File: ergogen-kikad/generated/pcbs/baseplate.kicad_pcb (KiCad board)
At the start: 2 copper layers, 111.1 x 55 mm, 22 parts, among them J1 Header clearance

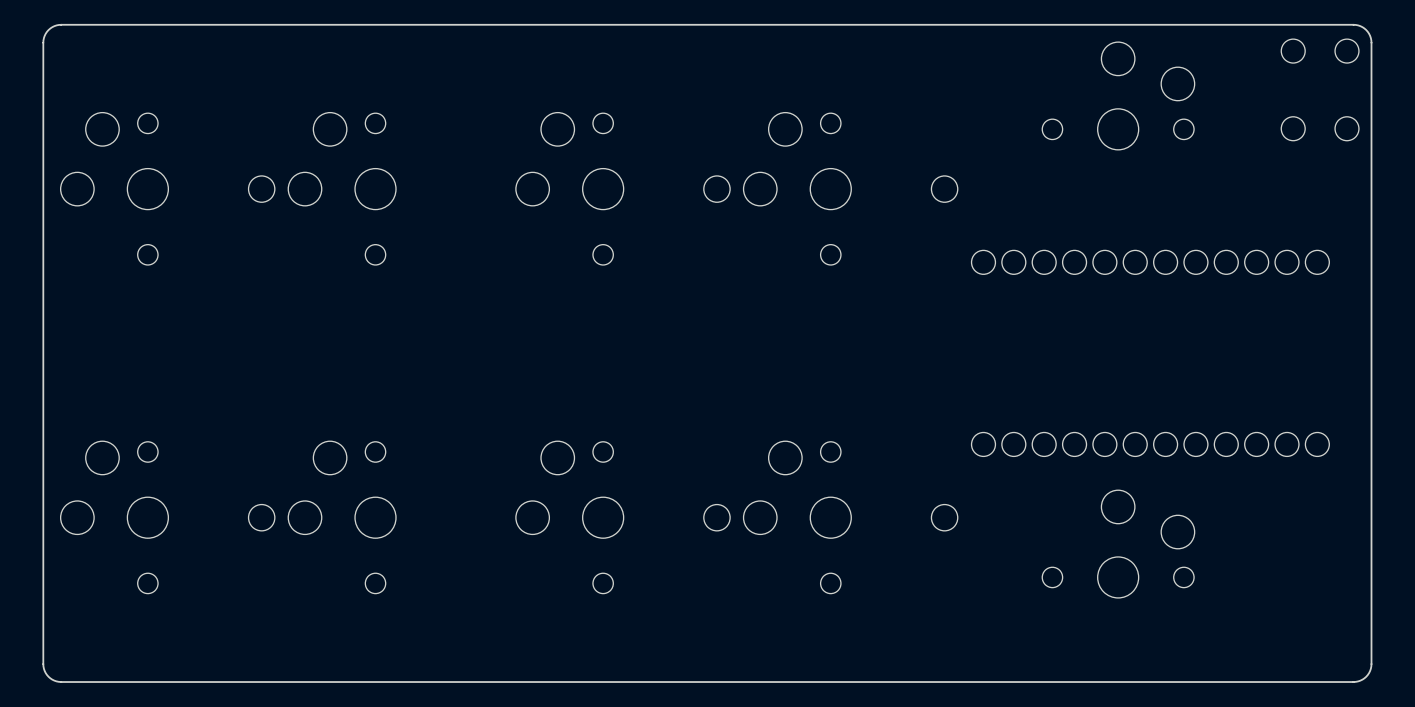
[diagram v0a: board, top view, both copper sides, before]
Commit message: Socket nice!view directly and lower reset button
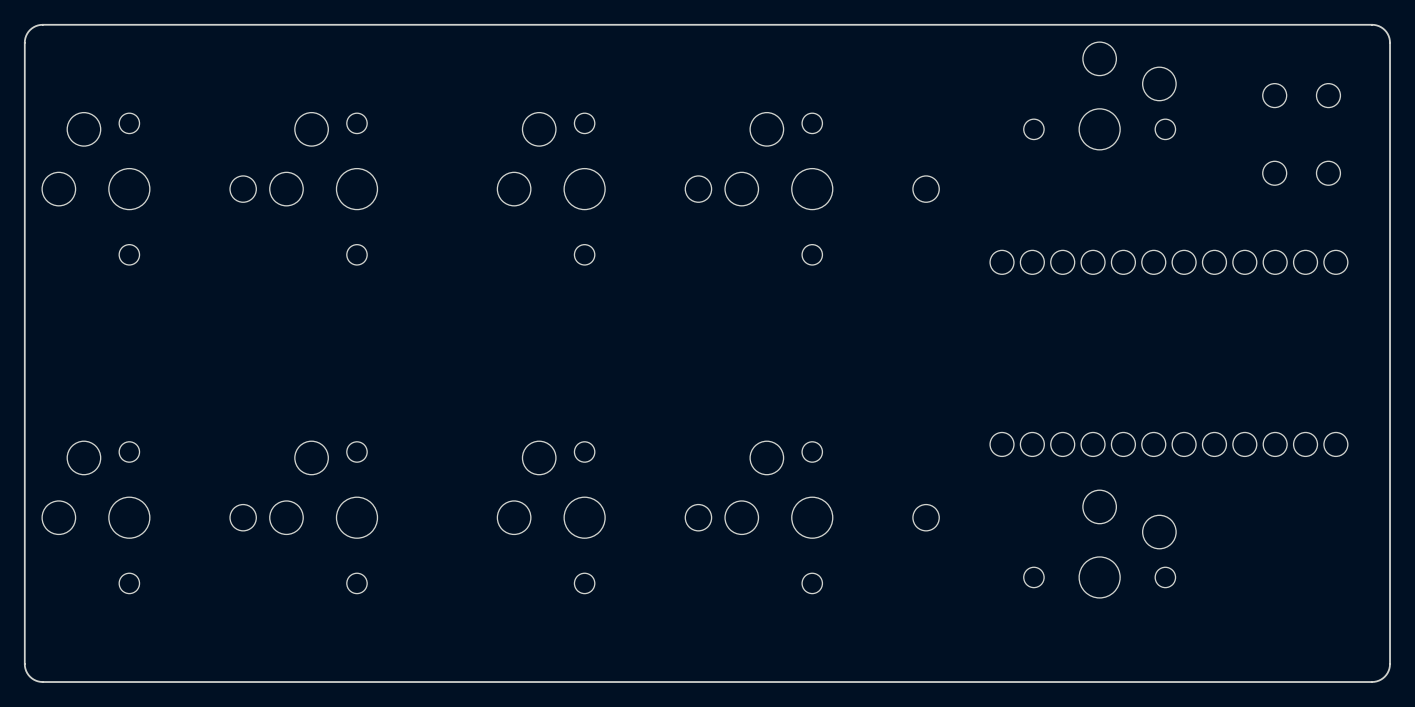
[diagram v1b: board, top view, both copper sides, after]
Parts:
- moved RST1 4.03 mm to (259.7, 130.2)
- moved BAT1 1.55 mm to (197.9, 148.5)
- moved H2 1.55 mm to (209.2, 134.8)
- moved H4 1.55 mm to (209.2, 162.2)
- moved J1 1.55 mm to (161.6, 162.2)
- moved LCD1 1.55 mm to (161.6, 162.2)
- moved MCU1 1.55 mm to (248.6, 148.5)
- moved PWR1 1.55 mm to (161.6, 162.2)
- moved S1 1.55 mm to (161.6, 134.8)
- moved S10 1.55 mm to (242.8, 167.2)
- moved S3 1.55 mm to (199.7, 134.8)
- moved S5 1.55 mm to (161.6, 162.2)
- moved S7 1.55 mm to (199.7, 162.2)
- moved S9 1.55 mm to (242.8, 129.8)
- moved H1 1.55 mm to (171.2, 134.8)
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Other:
- board size 111.1 x 55 mm -> 114.2 x 55 mm

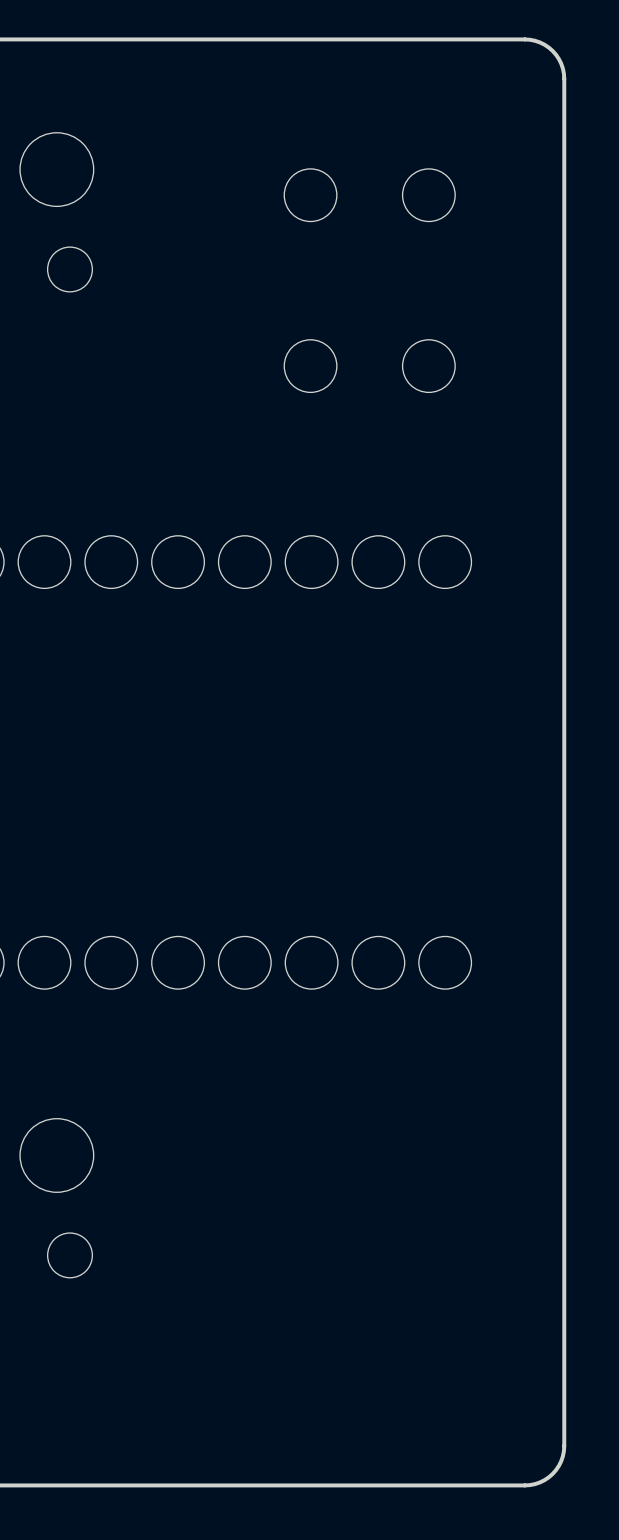
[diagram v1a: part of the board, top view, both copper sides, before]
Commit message: Align power and reset controls with column five keys
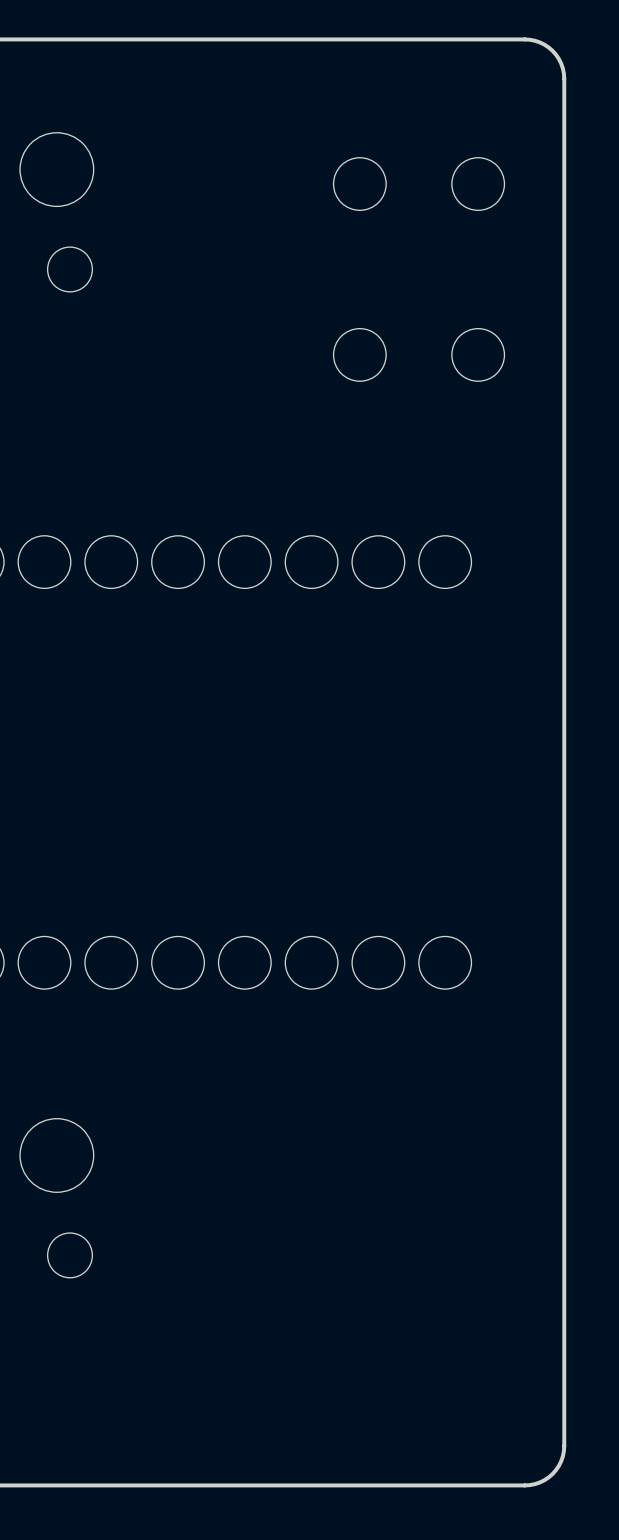
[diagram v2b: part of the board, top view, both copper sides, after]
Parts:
- moved RST1 1.92 mm to (261.6, 129.8)

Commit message: Mirror battery and connector within the central channel
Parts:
- moved BAT1 15.3 mm to (182.5, 148.5)
